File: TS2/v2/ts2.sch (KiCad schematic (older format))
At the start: 8 parts, among them U10 74LS32, U34 74LS00, U35 74LS74

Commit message: Add power switch.
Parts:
- added P3: +5V POWER, symbol CONN_01X02
- added SW5: POWER, symbol SPST
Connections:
- net GND: now also P3.1 (P1)
- net VCC: now also SW5.2
- new net: P3.2 (P2), SW5.1
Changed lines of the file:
@@
 Sheet 1 9
 Title "TS2 68000 Single Board Computer"
-Date "2017-01-14"
+Date "2017-01-15"
 Rev "2.0"
 Comp "Jeff Tranter"
@@
 L GND #PWR02
 U 1 1 57CB98A5
-P 2400 5450
-F 0 "#PWR02" H 2400 5200 50  0001 C CNN
-F 1 "GND" H 2400 5300 50  0000 C CNN
-F 2 "" H 2400 5450 50  0000 C CNN
-F 3 "" H 2400 5450 50  0000 C CNN
-	1    2400 5450
+P 1950 4700
+F 0 "#PWR02" H 1950 4450 50  0001 C CNN
+F 1 "GND" H 1950 4550 50  0000 C CNN
+F 2 "" H 1950 4700 50  0000 C CNN
+F 3 "" H 1950 4700 50  0000 C CNN
+	1    1950 4700
 	1    0    0    -1
 $EndComp
@@
 L PWR_FLAG #FLG04
 U 1 1 57CBBFC3
-P 2400 5450
-F 0 "#FLG04" H 2400 5545 50  0001 C CNN
-F 1 "PWR_FLAG" H 2400 5630 50  0000 C CNN
-F 2 "" H 2400 5450 50  0000 C CNN
-F 3 "" H 2400 5450 50  0000 C CNN
-	1    2400 5450
+P 1950 4700
+F 0 "#FLG04" H 1950 4795 50  0001 C CNN
+F 1 "PWR_FLAG" H 1950 4880 50  0000 C CNN
+F 2 "" H 1950 4700 50  0000 C CNN
+F 3 "" H 1950 4700 50  0000 C CNN
+	1    1950 4700
 	1    0    0    -1
 $EndComp
@@
 NoConn ~ 7950 4800
 NoConn ~ 7950 5200
+$Comp
+L CONN_01X02 P3
+U 1 1 587B85BD
+P 1950 5500
+F 0 "P3" H 1950 5650 50  0000 C CNN
+F 1 "+5V POWER" V 2050 5500 50  0000 C CNN
+F 2 "" H 1950 5500 50  0000 C CNN
+F 3 "" H 1950 5500 50  0000 C CNN
+	1    1950 5500
+	-1   0    0    1
+$EndComp
+$Comp
+L SPST SW5
+U 1 1 587B85F6
+P 2650 5450
+F 0 "SW5" H 2650 5550 50  0000 C CNN
+F 1 "POWER" H 2650 5350 50  0000 C CNN
+F 2 "" H 2650 5450 50  0000 C CNN
+F 3 "" H 2650 5450 50  0000 C CNN
+	1    2650 5450
+	1    0    0    -1
+$EndComp
+$Comp
+L VCC #PWR021
+U 1 1 587B86B5
+P 3150 5450
+F 0 "#PWR021" H 3150 5300 50  0001 C CNN
+F 1 "VCC" H 3150 5600 50  0000 C CNN
+F 2 "" H 3150 5450 50  0000 C CNN
+F 3 "" H 3150 5450 50  0000 C CNN
+	1    3150 5450
+	1    0    0    -1
+$EndComp
+$Comp
+L GND #PWR022
+U 1 1 587B86DD
+P 2150 5550
+F 0 "#PWR022" H 2150 5300 50  0001 C CNN
+F 1 "GND" H 2150 5400 50  0000 C CNN
+F 2 "" H 2150 5550 50  0000 C CNN
+F 3 "" H 2150 5550 50  0000 C CNN
+	1    2150 5550
+	1    0    0    -1
+$EndComp
 $EndSCHEMATC

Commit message: Fix up some issues with power supply circuitry.
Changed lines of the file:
@@
 Sheet 1 9
 Title "TS2 68000 Single Board Computer"
-Date "2017-01-15"
+Date "2017-01-19"
 Rev "2.0"
 Comp "Jeff Tranter"
@@
 	1    0    0    -1
 $EndComp
+Text GLabel 2550 6000 2    60   Input ~ 0
+POWER
+Wire Wire Line
+	2550 6000 2250 6000
+Wire Wire Line
+	2250 6000 2250 5450
+Connection ~ 2250 5450
 $EndSCHEMATC

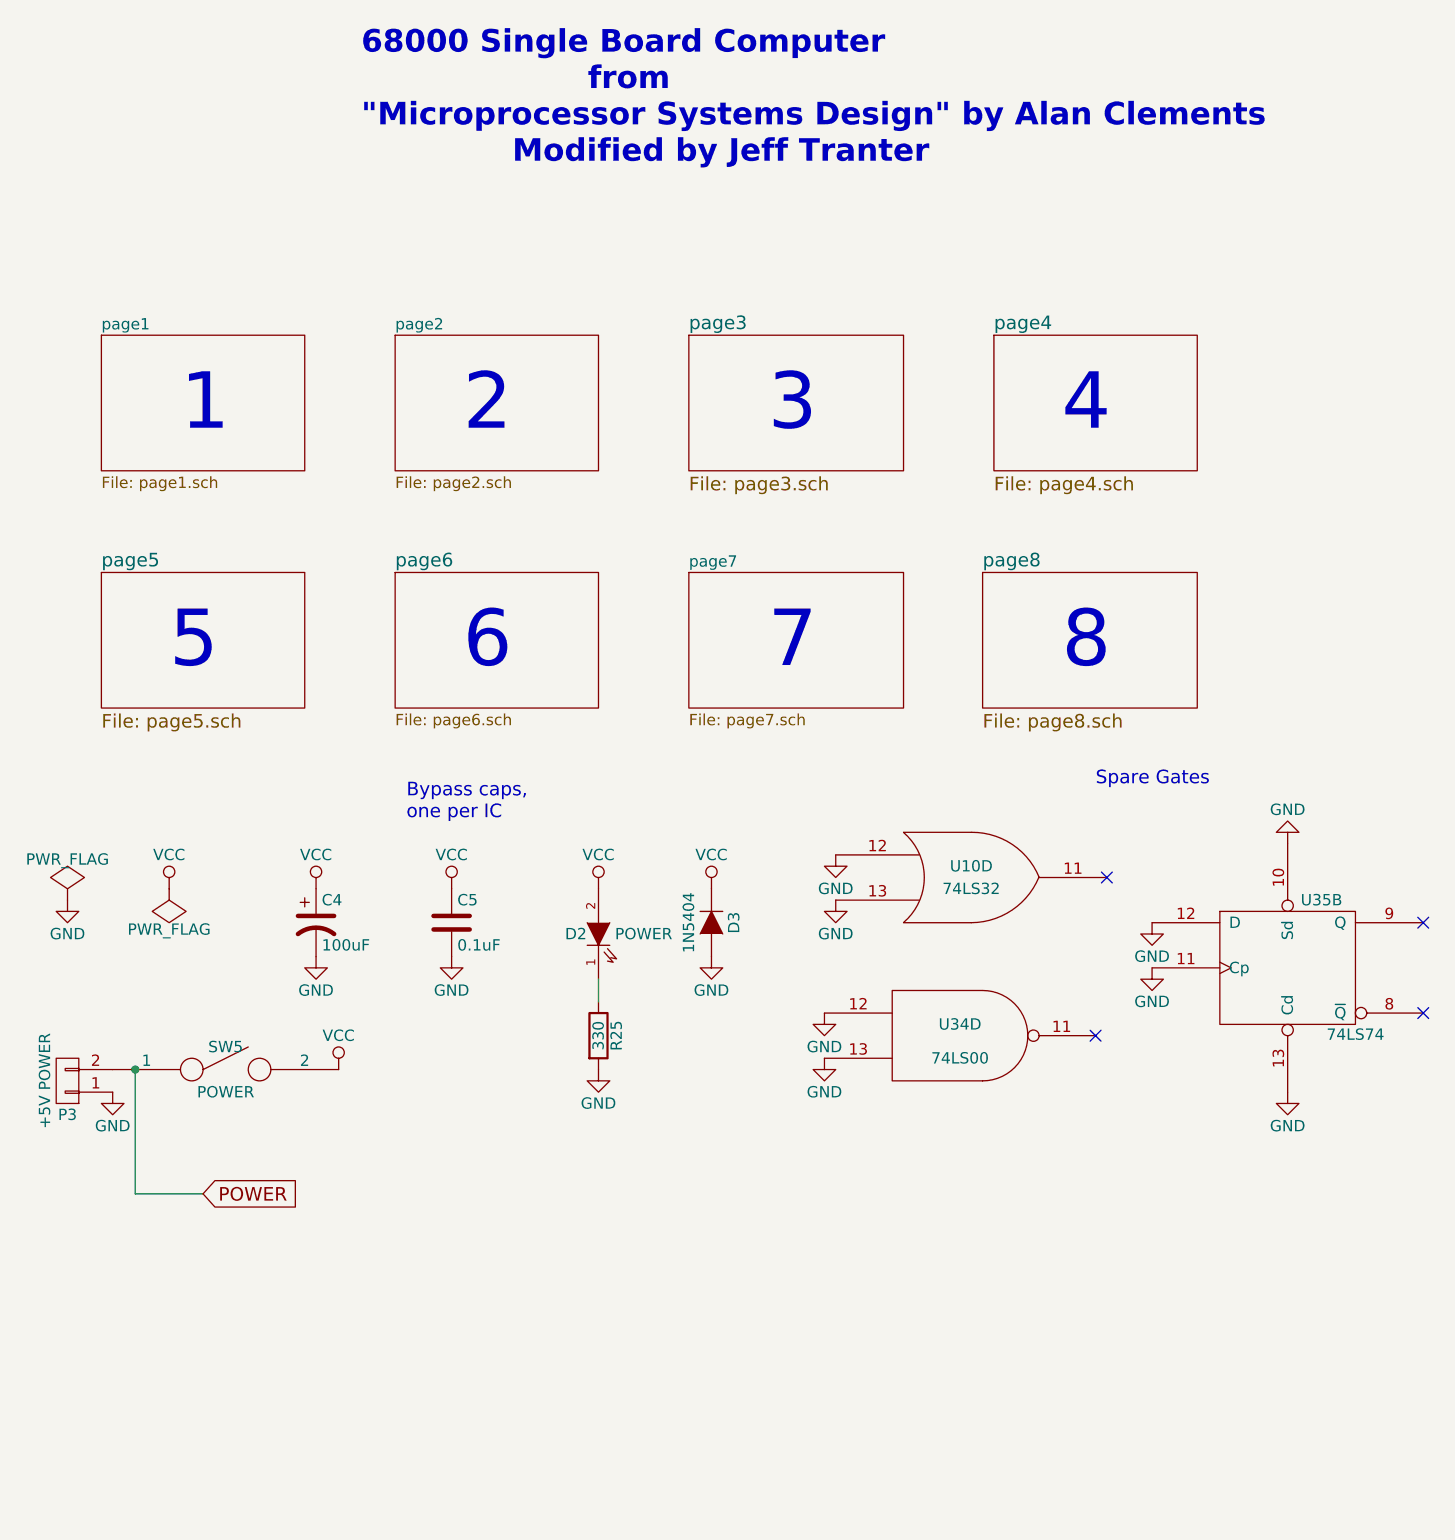
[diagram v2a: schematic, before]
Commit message: Add all bypass caps, show pullups as SIP resistors, start PCB layout.
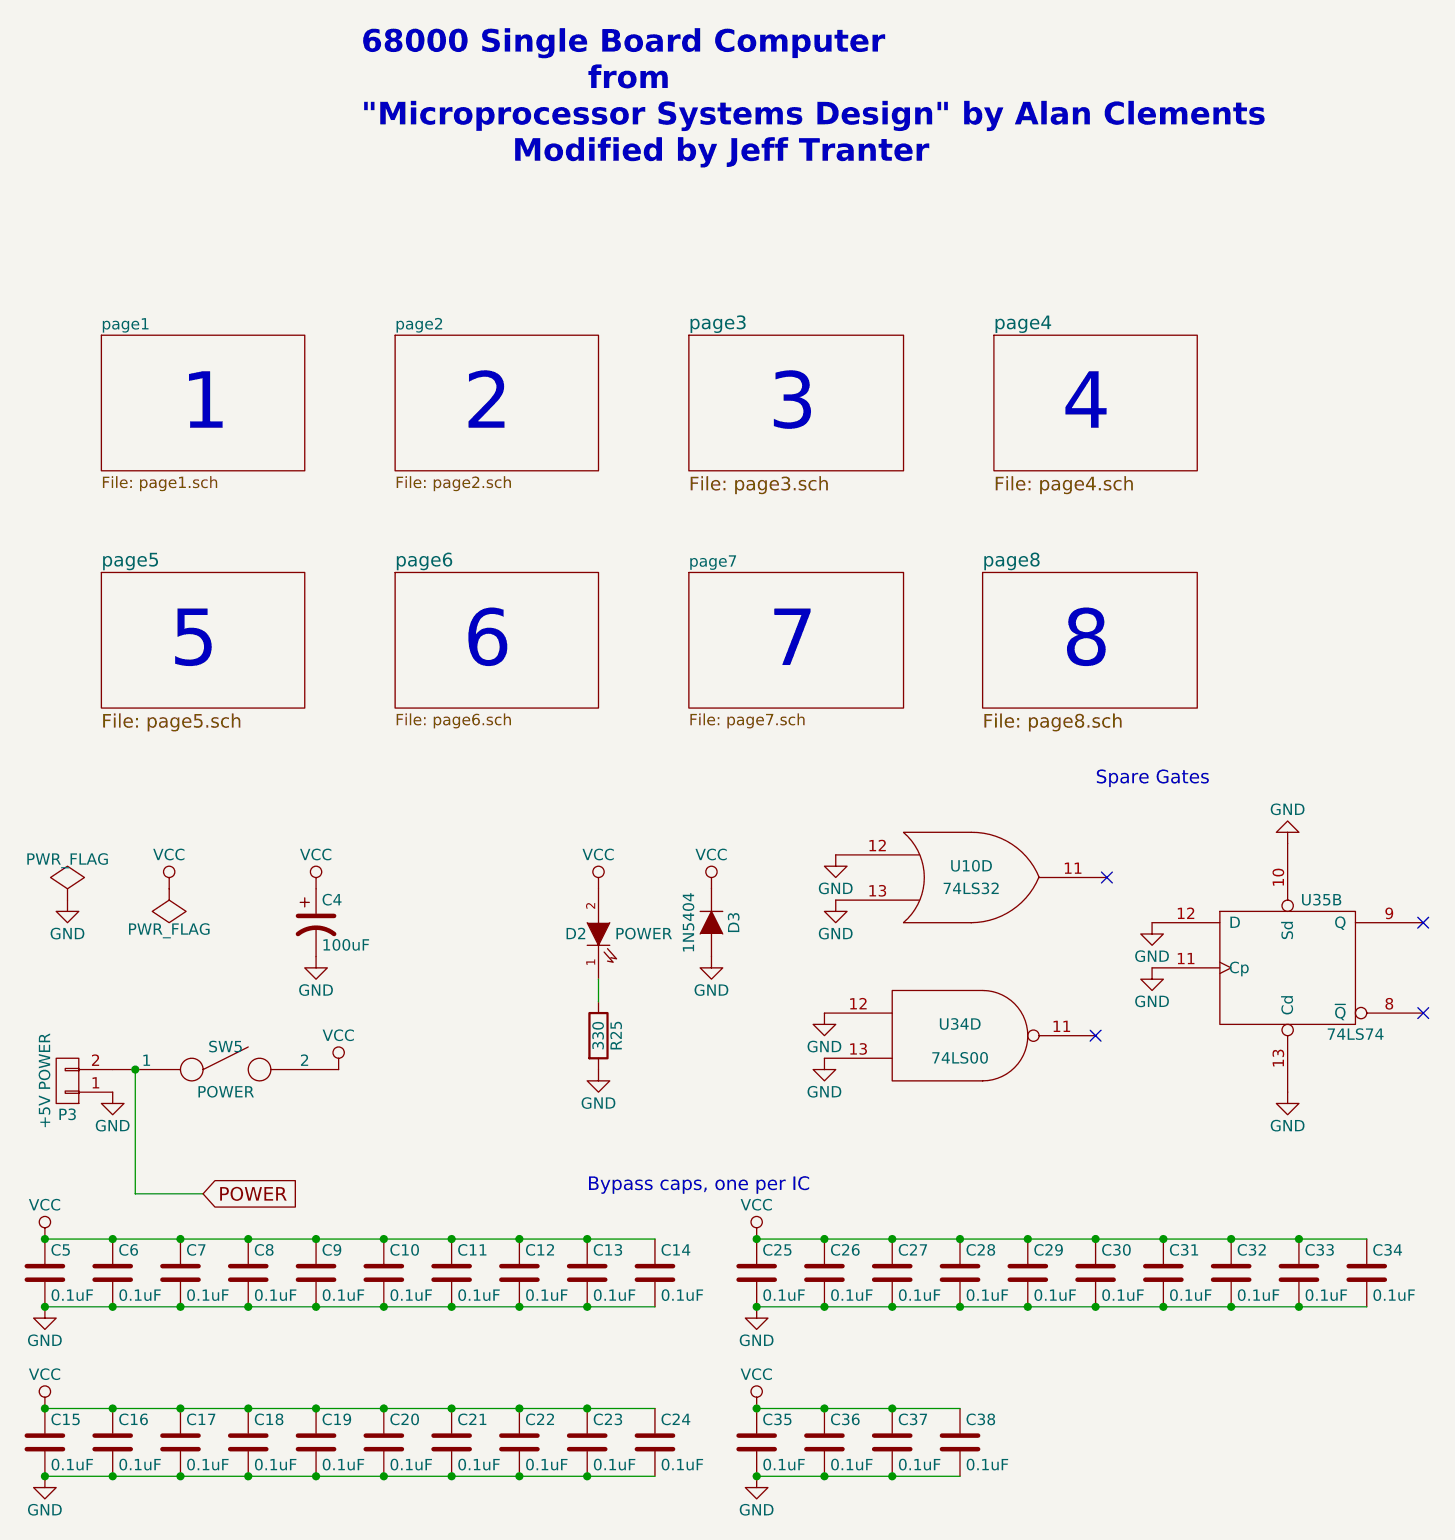
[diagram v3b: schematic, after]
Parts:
- added C10, C11, C12, C13, C14, C15, C16, C17, C18, C19, C20, C21, C22, C23, C24, C25, C26, C27, C28, C29, C30, C31, C32, C33, C34, C35, C36, C37, C38, C6, C7, C8, C9: 0.1uF, Capacitors_ThroughHole:C_Disc_D3_P2.5, symbol C
- C4: footprint (none) -> Capacitors_ThroughHole:C_Radial_D5_L6_P2.5
- C5: footprint (none) -> Capacitors_ThroughHole:C_Disc_D3_P2.5
- D2, P3: footprint (none) -> Connect:PINHEAD1-2
- D3: footprint (none) -> Diodes_ThroughHole:Diode_DO-35_SOD27_Horizontal_RM10
- R25: footprint (none) -> Resistors_ThroughHole:Resistor_Horizontal_RM7mm
- SW5: footprint (none) -> Connect:PINHEAD1-3
- U10, U34, U35: footprint (none) -> Housings_DIP:DIP-14_W7.62mm
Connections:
- net GND: now also C10.2, C11.2, C12.2, C13.2, C14.2, C15.2, C16.2, C17.2, C18.2, C19.2, C20.2, C21.2, C22.2, C23.2, C24.2, C25.2, C26.2, C27.2, C28.2, C29.2, C30.2, C31.2, C32.2, C33.2, C34.2, C35.2, C36.2, C37.2, C38.2, C6.2, C7.2, C8.2, C9.2
- net VCC: now also C10.1, C11.1, C12.1, C13.1, C14.1, C15.1, C16.1, C17.1, C18.1, C19.1, C20.1, C21.1, C22.1, C23.1, C24.1, C25.1, C26.1, C27.1, C28.1, C29.1, C30.1, C31.1, C32.1, C33.1, C34.1, C35.1, C36.1, C37.1, C38.1, C6.1, C7.1, C8.1, C9.1
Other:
- note added: "Bypass caps, one per IC"
- note removed: "Bypass caps,\none per IC"
- moved on the sheet: C5
